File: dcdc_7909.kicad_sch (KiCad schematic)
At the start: 60 parts, among them J1 V_IN, J2 G_IN, J3 RFShield_Clip, J4 RFShield_Clip, J5 RFShield_Clip, J6 RFShield_Clip, J7 +10V, J8 G_OUT, J9 -10V, U1 LM2940-SOT223-15, U2 LT3471, U3 LT3045xMSE, U4 LT3094xMSE

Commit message: Rev 2.1 finished.
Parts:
- C12: value 470p -> 150p; LCSC C1620 -> C1527
- C14, C21, C23, C9: LCSC C57112 -> C15195
- C17, C18: value 10u -> 22u; footprint Capacitor_SMD:C_0805_2012Metric -> Capacitor_SMD:C_1206_3216Metric; LCSC C15850 -> C12891; PN (none) -> Samsung CL31A226KAHNNNE
- C5: LCSC C14663 -> C307331
- C6: value 2200p -> 150p; LCSC C1604 -> C1527
- R1: LCSC C4184 -> C25765
- R2, R4: value DNP -> 2k; LCSC DO NOT POPULATE -> C4109
- R3: value 18k -> 20k; LCSC C25810 -> C25765
- R5: value 2k -> DNP; LCSC C22975 -> DO NOT POPULATE
- R6: value 20k -> 22k; LCSC C4184 -> C25768
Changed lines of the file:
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@@
       (effects (font (size 1.27 1.27)) (justify left))
     )
-    (property "Value" "10u" (id 1) (at 182.6768 112.268 0)
-      (effects (font (size 1.27 1.27)) (justify left))
-    )
-    (property "Footprint" "Capacitor_SMD:C_0805_2012Metric" (id 2) (at 180.34 111.125 0)
+    (property "Value" "22u" (id 1) (at 182.6768 112.268 0)
+      (effects (font (size 1.27 1.27)) (justify left))
+    )
+    (property "Footprint" "Capacitor_SMD:C_1206_3216Metric" (id 2) (at 180.34 111.125 0)
       (effects (font (size 1.27 1.27)) hide)
     )
@@
       (effects (font (size 1.27 1.27)) hide)
     )
-    (property "LCSC" "C15850" (id 4) (at 180.34 111.125 0)
+    (property "LCSC" "C12891" (id 4) (at 180.34 111.125 0)
+      (effects (font (size 1.27 1.27)) hide)
+    )
+    (property "PN" "Samsung CL31A226KAHNNNE" (id 5) (at 180.34 111.125 0)
       (effects (font (size 1.27 1.27)) hide)
     )
@@
       (effects (font (size 1.27 1.27)) (justify left))
     )
-    (property "Value" "10u" (id 1) (at 183.9468 72.898 0)
-      (effects (font (size 1.27 1.27)) (justify left))
-    )
-    (property "Footprint" "Capacitor_SMD:C_0805_2012Metric" (id 2) (at 181.61 71.755 0)
+    (property "Value" "22u" (id 1) (at 183.9468 72.898 0)
+      (effects (font (size 1.27 1.27)) (justify left))
+    )
+    (property "Footprint" "Capacitor_SMD:C_1206_3216Metric" (id 2) (at 181.61 71.755 0)
       (effects (font (size 1.27 1.27)) hide)
     )
@@
       (effects (font (size 1.27 1.27)) hide)
     )
-    (property "LCSC" "C15850" (id 4) (at 181.61 71.755 0)
+    (property "LCSC" "C12891" (id 4) (at 181.61 71.755 0)
+      (effects (font (size 1.27 1.27)) hide)
+    )
+    (property "PN" "Samsung CL31A226KAHNNNE" (id 5) (at 181.61 71.755 0)
       (effects (font (size 1.27 1.27)) hide)
     )
@@
       (effects (font (size 1.27 1.27)) hide)
     )
-    (property "LCSC" "C57112" (id 4) (at 238.76 65.405 0)
+    (property "LCSC" "C15195" (id 4) (at 238.76 65.405 0)
       (effects (font (size 1.27 1.27)) hide)
     )
@@
       (effects (font (size 1.27 1.27)) hide)
     )
-    (property "LCSC" "C57112" (id 4) (at 248.92 103.505 0)
+    (property "LCSC" "C15195" (id 4) (at 248.92 103.505 0)
       (effects (font (size 1.27 1.27)) hide)
     )
@@
       (effects (font (size 1.27 1.27)) hide)
     )
-    (property "LCSC" "C4184" (id 4) (at 50.8 123.825 0)
+    (property "LCSC" "C25765" (id 4) (at 50.8 123.825 0)
       (effects (font (size 1.27 1.27)) hide)
     )
@@
       (effects (font (size 1.27 1.27)) (justify left))
     )
-    (property "Value" "DNP" (id 1) (at 109.728 107.823 0)
+    (property "Value" "2k" (id 1) (at 109.728 107.823 0)
       (effects (font (size 1.27 1.27)) (justify left))
     )
@@
       (effects (font (size 1.27 1.27)) hide)
     )
-    (property "LCSC" "DO NOT POPULATE" (id 4) (at 108.585 106.045 0)
+    (property "LCSC" "C4109" (id 4) (at 108.585 106.045 0)
       (effects (font (size 1.27 1.27)) hide)
     )
@@
       (effects (font (size 1.27 1.27)) hide)
     )
-    (property "LCSC" "C14663" (id 4) (at 73.66 152.4 0)
+    (property "LCSC" "C307331" (id 4) (at 73.66 152.4 0)
       (effects (font (size 1.27 1.27)) hide)
     )
@@
       (effects (font (size 1.27 1.27)) (justify left))
     )
-    (property "Value" "2k" (id 1) (at 109.728 114.173 0)
+    (property "Value" "DNP" (id 1) (at 109.728 114.173 0)
       (effects (font (size 1.27 1.27)) (justify left))
     )
@@
       (effects (font (size 1.27 1.27)) hide)
     )
-    (property "LCSC" "C22975" (id 4) (at 108.585 112.395 0)
+    (property "LCSC" "DO NOT POPULATE" (id 4) (at 108.585 112.395 0)
       (effects (font (size 1.27 1.27)) hide)
     )
@@
       (effects (font (size 1.27 1.27)) (justify left))
     )
-    (property "Value" "20k" (id 1) (at 123.317 86.487 0)
+    (property "Value" "22k" (id 1) (at 123.317 86.487 0)
       (effects (font (size 1.27 1.27)) (justify left))
     )
@@
       (effects (font (size 1.27 1.27)) hide)
     )
-    (property "LCSC" "C4184" (id 4) (at 125.095 87.63 0)
+    (property "LCSC" "C25768" (id 4) (at 125.095 87.63 0)
       (effects (font (size 1.27 1.27)) hide)
     )
@@
       (effects (font (size 1.27 1.27)) (justify left))
     )
-    (property "Value" "470p" (id 1) (at 132.5118 88.773 0)
+    (property "Value" "150p" (id 1) (at 132.5118 88.773 0)
       (effects (font (size 1.27 1.27)) (justify left))
     )
@@
       (effects (font (size 1.27 1.27)) hide)
     )
-    (property "LCSC" "C1620" (id 4) (at 130.175 87.63 0)
+    (property "LCSC" "C1527" (id 4) (at 130.175 87.63 0)
       (effects (font (size 1.27 1.27)) hide)
     )
@@
       (effects (font (size 1.27 1.27)) hide)
     )
-    (property "LCSC" "C57112" (id 4) (at 89.535 95.25 0)
+    (property "LCSC" "C15195" (id 4) (at 89.535 95.25 0)
       (effects (font (size 1.27 1.27)) hide)
     )
@@
       (effects (font (size 1.27 1.27)) hide)
     )
-    (property "LCSC" "C57112" (id 4) (at 148.59 87.63 0)
+    (property "LCSC" "C15195" (id 4) (at 148.59 87.63 0)
       (effects (font (size 1.27 1.27)) hide)
     )
@@
       (effects (font (size 1.27 1.27)) (justify left))
     )
-    (property "Value" "18k" (id 1) (at 68.707 96.012 0)
+    (property "Value" "20k" (id 1) (at 68.707 96.012 0)
       (effects (font (size 1.27 1.27)) (justify left))
     )
@@
       (effects (font (size 1.27 1.27)) hide)
     )
-    (property "LCSC" "C25810" (id 4) (at 70.485 97.155 0)
+    (property "LCSC" "C25765" (id 4) (at 70.485 97.155 0)
       (effects (font (size 1.27 1.27)) hide)
     )
@@
       (effects (font (size 1.27 1.27)) (justify left))
     )
-    (property "Value" "DNP" (id 1) (at 68.453 144.272 0)
+    (property "Value" "2k" (id 1) (at 68.453 144.272 0)
       (effects (font (size 1.27 1.27)) (justify left))
     )
@@
       (effects (font (size 1.27 1.27)) hide)
     )
-    (property "LCSC" "DO NOT POPULATE" (id 4) (at 66.675 145.415 0)
+    (property "LCSC" "C4109" (id 4) (at 66.675 145.415 0)
       (effects (font (size 1.27 1.27)) hide)
     )
@@
       (effects (font (size 1.27 1.27)) (justify left))
     )
-    (property "Value" "2200p" (id 1) (at 77.9018 98.298 0)
+    (property "Value" "150p" (id 1) (at 77.9018 98.298 0)
       (effects (font (size 1.27 1.27)) (justify left))
     )
@@
       (effects (font (size 1.27 1.27)) hide)
     )
-    (property "LCSC" "C1604" (id 4) (at 75.565 97.155 0)
+    (property "LCSC" "C1527" (id 4) (at 75.565 97.155 0)
       (effects (font (size 1.27 1.27)) hide)
     )
@@
     )
     (path "/efffde45-ed55-4b24-8009-16a95de1f75d"
-      (reference "C6") (unit 1) (value "2200p") (footprint "Capacitor_SMD:C_0402_1005Metric")
+      (reference "C6") (unit 1) (value "150p") (footprint "Capacitor_SMD:C_0402_1005Metric")
     )
     (path "/33c03a2e-c7c0-4ac0-8b58-0f5daee7b249"
@@
     )
     (path "/6e0ed22c-ecdc-40a8-afb4-ac6ef4db0660"
-      (reference "C12") (unit 1) (value "470p") (footprint "Capacitor_SMD:C_0402_1005Metric")
+      (reference "C12") (unit 1) (value "150p") (footprint "Capacitor_SMD:C_0402_1005Metric")
     )
     (path "/0703d55f-cdae-441a-870f-e2fd578f5c07"
@@
     )
     (path "/00000000-0000-0000-0000-00005ea20b33"
-      (reference "C17") (unit 1) (value "10u") (footprint "Capacitor_SMD:C_0805_2012Metric")
+      (reference "C17") (unit 1) (value "22u") (footprint "Capacitor_SMD:C_1206_3216Metric")
     )
     (path "/00000000-0000-0000-0000-00005ea22de1"
-      (reference "C18") (unit 1) (value "10u") (footprint "Capacitor_SMD:C_0805_2012Metric")
+      (reference "C18") (unit 1) (value "22u") (footprint "Capacitor_SMD:C_1206_3216Metric")
     )
     (path "/00000000-0000-0000-0000-00005ea1a7bc"
@@
     )
     (path "/e29e1d4b-3efc-442d-a920-0534eba44ce1"
-      (reference "R2") (unit 1) (value "DNP") (footprint "Resistor_SMD:R_0402_1005Metric")
+      (reference "R2") (unit 1) (value "2k") (footprint "Resistor_SMD:R_0402_1005Metric")
     )
     (path "/90e51816-a1d4-45a7-942c-682d8cce5b3b"
-      (reference "R3") (unit 1) (value "18k") (footprint "Resistor_SMD:R_0402_1005Metric")
+      (reference "R3") (unit 1) (value "20k") (footprint "Resistor_SMD:R_0402_1005Metric")
     )
     (path "/0256f1b1-bf8f-4009-b7af-3fbb7136a850"
-      (reference "R4") (unit 1) (value "DNP") (footprint "Resistor_SMD:R_0402_1005Metric")
+      (reference "R4") (unit 1) (value "2k") (footprint "Resistor_SMD:R_0402_1005Metric")
     )
     (path "/18aa7285-da5c-42b6-a485-257c708a9352"
-      (reference "R5") (unit 1) (value "2k") (footprint "Resistor_SMD:R_0402_1005Metric")
+      (reference "R5") (unit 1) (value "DNP") (footprint "Resistor_SMD:R_0402_1005Metric")
     )
     (path "/3090092e-4c9a-4661-95c3-730de5416b81"
-      (reference "R6") (unit 1) (value "20k") (footprint "Resistor_SMD:R_0402_1005Metric")
+      (reference "R6") (unit 1) (value "22k") (footprint "Resistor_SMD:R_0402_1005Metric")
     )
     (path "/00000000-0000-0000-0000-00005ea01b91"

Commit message: Final v2.1.
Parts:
- R2, R4: value 2k -> 2k05; LCSC C4109 -> C852693
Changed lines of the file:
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@@
       (effects (font (size 1.27 1.27)) (justify left))
     )
-    (property "Value" "2k" (id 1) (at 109.728 107.823 0)
+    (property "Value" "2k05" (id 1) (at 109.728 107.823 0)
       (effects (font (size 1.27 1.27)) (justify left))
     )
@@
       (effects (font (size 1.27 1.27)) hide)
     )
-    (property "LCSC" "C4109" (id 4) (at 108.585 106.045 0)
+    (property "LCSC" "C852693" (id 4) (at 108.585 106.045 0)
       (effects (font (size 1.27 1.27)) hide)
     )
@@
       (effects (font (size 1.27 1.27)) (justify left))
     )
-    (property "Value" "2k" (id 1) (at 68.453 144.272 0)
+    (property "Value" "2k05" (id 1) (at 68.453 144.272 0)
       (effects (font (size 1.27 1.27)) (justify left))
     )
@@
       (effects (font (size 1.27 1.27)) hide)
     )
-    (property "LCSC" "C4109" (id 4) (at 66.675 145.415 0)
+    (property "LCSC" "C852693" (id 4) (at 66.675 145.415 0)
       (effects (font (size 1.27 1.27)) hide)
     )
@@
     )
     (path "/e29e1d4b-3efc-442d-a920-0534eba44ce1"
-      (reference "R2") (unit 1) (value "2k") (footprint "Resistor_SMD:R_0402_1005Metric")
+      (reference "R2") (unit 1) (value "2k05") (footprint "Resistor_SMD:R_0402_1005Metric")
     )
     (path "/90e51816-a1d4-45a7-942c-682d8cce5b3b"
@@
     )
     (path "/0256f1b1-bf8f-4009-b7af-3fbb7136a850"
-      (reference "R4") (unit 1) (value "2k") (footprint "Resistor_SMD:R_0402_1005Metric")
+      (reference "R4") (unit 1) (value "2k05") (footprint "Resistor_SMD:R_0402_1005Metric")
     )
     (path "/18aa7285-da5c-42b6-a485-257c708a9352"

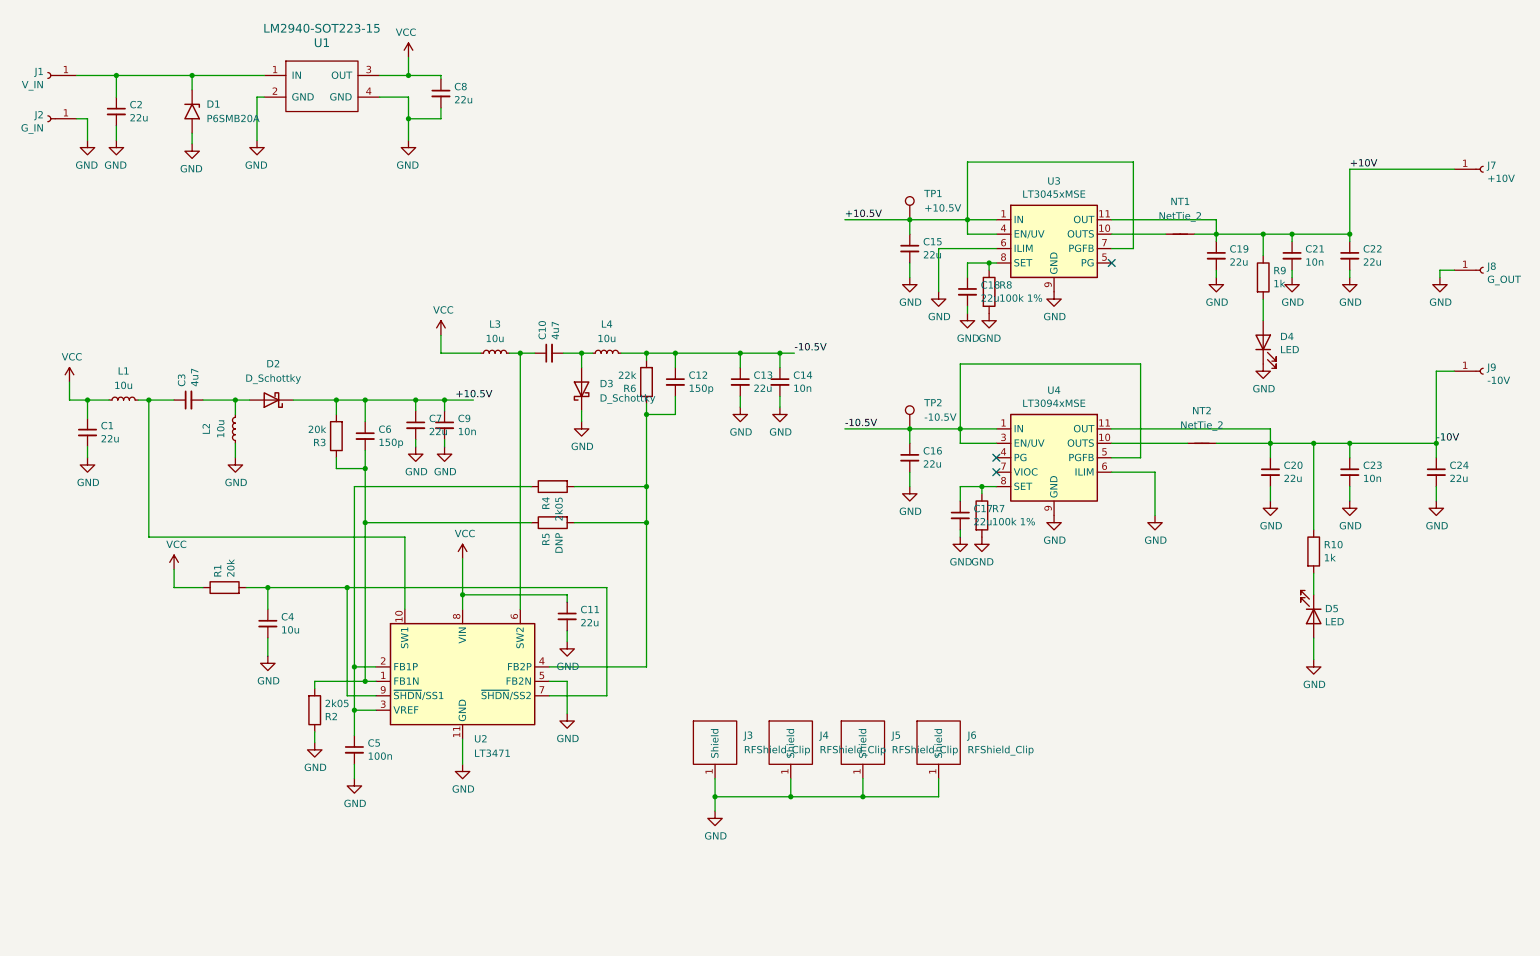
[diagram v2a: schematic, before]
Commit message: Reworking the board with MAX76x/
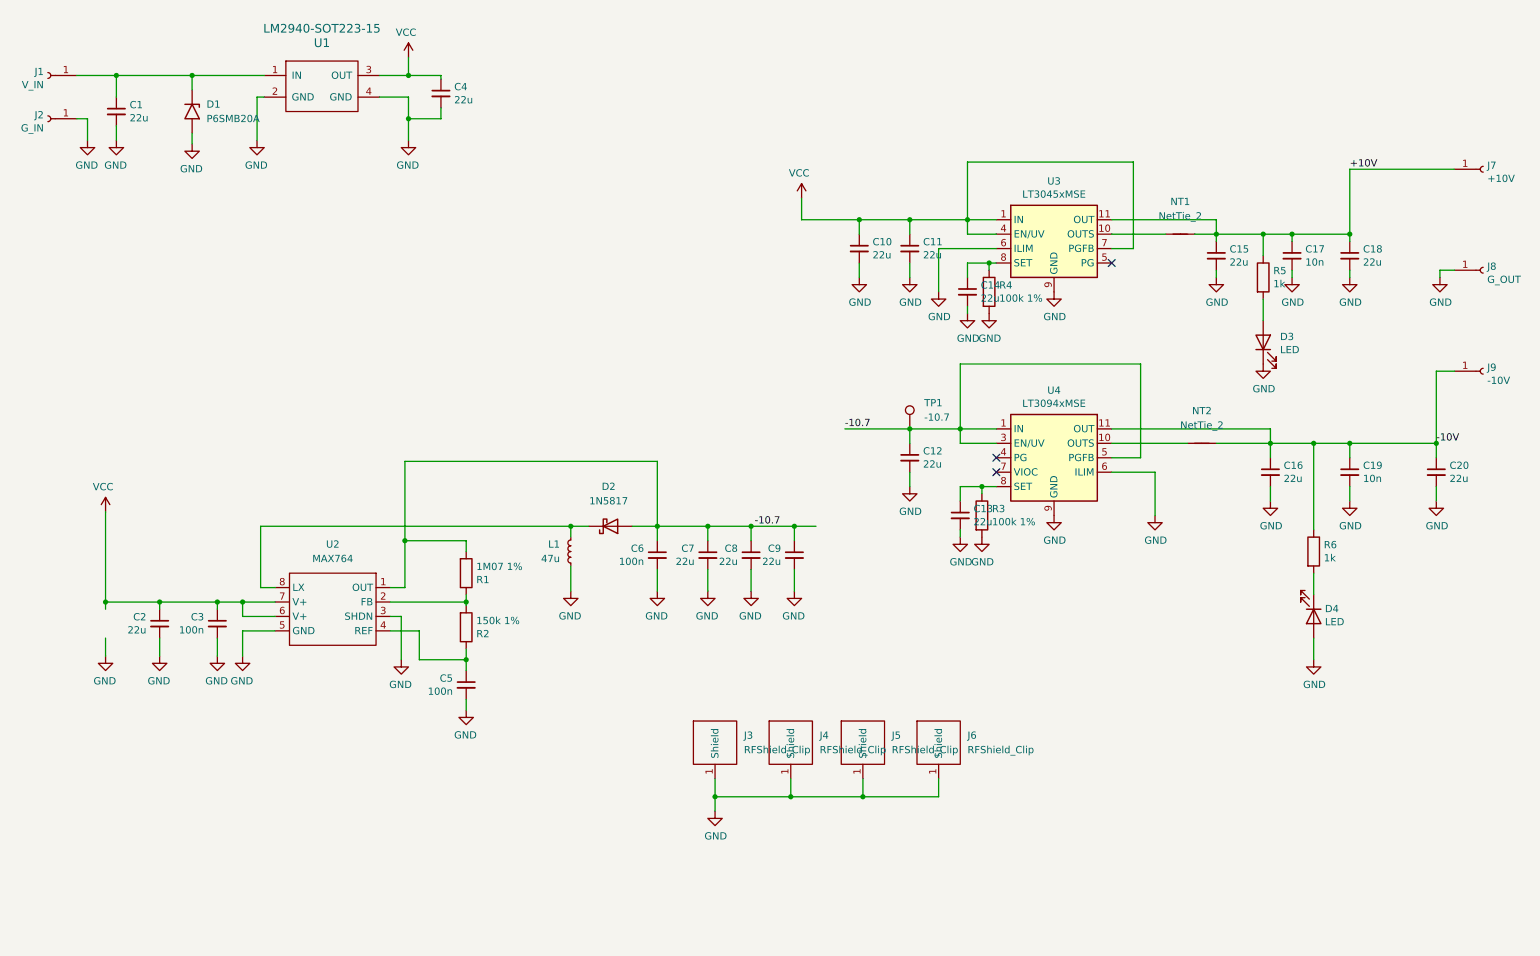
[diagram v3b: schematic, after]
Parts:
- removed C11, C13: 22u, Capacitor_SMD:C_1210_3225Metric, symbol Device:C_Small
- removed C12: 150p, Capacitor_SMD:C_0402_1005Metric, symbol Device:C_Small
- removed C14: 10n, Capacitor_SMD:C_0402_1005Metric, symbol Device:C_Small
- removed C4: 10u, Capacitor_SMD:C_0603_1608Metric, symbol Device:C_Small
- removed D2, D3: D_Schottky, Diode_SMD:D_PowerDI-123, symbol Device:D_Schottky
- removed L2, L3, L4: 10u, Inductor_SMD:L_Vishay_IHLP-1616, symbol Device:L_Small
- removed R3: 20k, Resistor_SMD:R_0402_1005Metric, symbol Device:R
- removed R4: 2k05, Resistor_SMD:R_0402_1005Metric, symbol Device:R
- removed R5: DNP, Resistor_SMD:R_0402_1005Metric, symbol Device:R
- removed R6: 22k, Resistor_SMD:R_0402_1005Metric, symbol Device:R
- removed TP1: +10.5V, TestPoint:TestPoint_THTPad_D1.0mm_Drill0.5mm, symbol Connector:TestPoint
- removed U2: LT3471, Package_DFN_QFN:DFN-10-1EP_3x3mm_P0.5mm_EP1.65x2.38mm, symbol Regulator_Switching:LT3471
- added C8: 22u, Capacitor_SMD:C_1210_3225Metric, symbol Device:C_Small
- added D2: 1N5817, Diode_SMD:D_SOD-123, symbol Diode:1N5817
- added U2: MAX764, Package_SO:SO-8_3.9x4.9mm_P1.27mm, symbol marcin_library:MAX764
- C10: value 4u7 -> 22u; footprint Capacitor_SMD:C_1206_3216Metric -> Capacitor_SMD:C_1210_3225Metric; LCSC C29823 -> C426653; PN (none) -> Murata GCM32EC71E226KE36
- C3: value 4u7 -> 100n; footprint Capacitor_SMD:C_1206_3216Metric -> Capacitor_SMD:C_0402_1005Metric; LCSC C29823 -> C15195
- C5: LCSC C307331 -> C15195
- C6: value 150p -> 100n; LCSC C1527 -> C15195
- C9: value 10n -> 22u; footprint Capacitor_SMD:C_0402_1005Metric -> Capacitor_SMD:C_1210_3225Metric; LCSC C15195 -> C426653; PN (none) -> Murata GCM32EC71E226KE36
- L1: value 10u -> 47u; footprint Inductor_SMD:L_Vishay_IHLP-1616 -> Inductor_SMD:L_Taiyo-Yuden_NR-60xx; LCSC C878322 -> (none)
- R1: value 20k -> 1M07 1%; footprint Resistor_SMD:R_0402_1005Metric -> Resistor_SMD:R_0603_1608Metric; LCSC C25765 -> C25803
- R2: value 2k05 -> 150k 1%; footprint Resistor_SMD:R_0402_1005Metric -> Resistor_SMD:R_0603_1608Metric; LCSC C852693 -> C25803
- TP1: renamed from TP2; value -10.5V -> -10.7
- renumbered C2 to C1, C15 to C11, C16 to C12, C17 to C13, C18 to C14, C19 to C15, C20 to C16, C21 to C17, C22 to C18, C23 to C19, C1 to C2, C24 to C20, C8 to C4, D4 to D3, D5 to D4, R7 to R3, R8 to R4, R9 to R5, R10 to R6
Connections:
- net -10.5V is gone; now on net -10.7: C12.1, TP1.1, U4.1 (IN), U4.13 (IN), U4.2 (IN), U4.3 (EN/UV), U4.5 (PGFB)
- net GND: now also C10.2, C3.2, C6.2, L1.2, C8.2, U2.3 (SHDN), U2.5 (GND); no longer R2.1
- net VCC: now also C10.1, C11.1, C3.1, U3.1 (IN), U3.2 (IN), U3.3 (IN), U3.4 (EN/UV), U3.7 (PGFB), U2.6 (V+), U2.7 (V+); no longer L1.1, R1.1
- net -10.7: now reaches R1.2
- net -10.7: now also C6.1, C7.1, C9.1, C8.1, D2.2 (A), U2.1 (OUT)
- net at C5.1: now also R2.1, U2.4 (REF)
- net at R2.2: now also R1.1, U2.2 (FB); no longer C6.2
- removed net +10.5V: C11.1, C6.1, C7.1, C9.1, U3.1 (IN), U3.2 (IN), U3.3 (IN), U3.4 (EN/UV), U3.7 (PGFB)
- new net: D2.1 (K), L1.1, U2.8 (LX)
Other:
- moved on the sheet: C2

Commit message: Reworking almost completed.
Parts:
- removed J3, J4, J5, J6: RFShield_Clip, marcin_library:S0971-46R, symbol marcin_library:RFShield_Clip
- added C1: 22u, Capacitor_SMD:C_1210_3225Metric, symbol Device:C_Small
- added J3, J4, J5, J6: Conn_01x01, Connector_Wire:SolderWirePad_1x01_SMD_1x2mm, symbol Connector_Generic:Conn_01x01
- D2: footprint Diode_SMD:D_SOD-123 -> Diode_SMD:D_PowerDI-123
- R1, R2, R5, R6: footprint Resistor_SMD:R_0603_1608Metric -> Resistor_SMD:R_0402_1005Metric
- renumbered C9 to C10, C10 to C11, C11 to C12, C12 to C13, C13 to C14, C14 to C15, C15 to C16, C16 to C17, C17 to C18, C18 to C19, C1 to C2, C19 to C20, C20 to C21, C2 to C3, C3 to C4, C4 to C5, C5 to C6, C6 to C7, C7 to C8, C8 to C9
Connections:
- net GND: now also C1.2, J3.1 (Pin_1), J4.1 (Pin_1), J5.1 (Pin_1), J6.1 (Pin_1)
- net VCC: now also C1.1
- net FB: now reaches R1.1, R2.2, U2.2 (FB)
